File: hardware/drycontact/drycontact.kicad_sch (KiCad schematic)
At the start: 0 parts

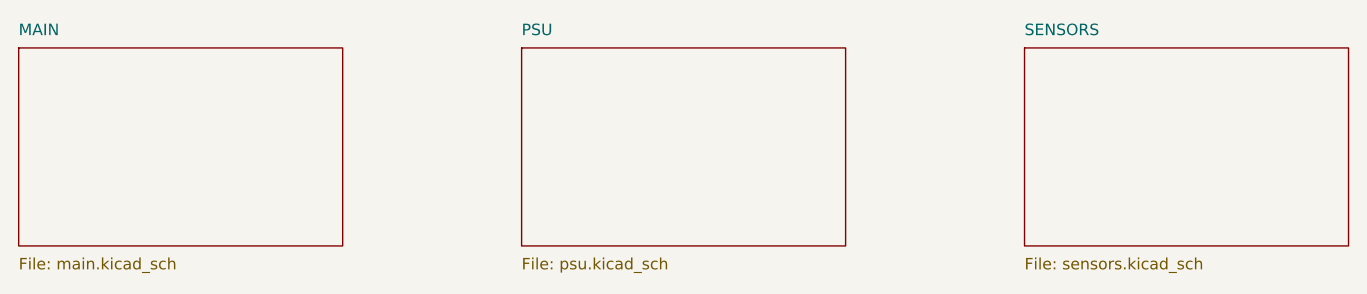
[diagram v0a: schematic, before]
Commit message: hardware: place parts for DryContact, PlugControl, SensorBuddy
Generate each board's schematic from a scripts/<board>.schgen.py manifest —
every part resolves to a real KiCad symbol + matching footprint + 3D model + LCSC.
Parts are PLACED, not wired (wire in eeschema; each sheet carries a pinout note).
make check-<board> = structure sound for all three:
- DryContact  (NEW): 49 components — STM32G0B1 + TCAN1044 + ULN2003 + 4x Omron
  G6K-2F-Y Form-C dry contacts; 29-bit CAN, UID auto-address. + BOM + handsolder.
- PlugControl (NEW KiCad project): 88 components — mcu/safety/actuation. A few
  generic stand-in symbols (TLV3202/74HC08/REF3330/TPS3823/SSR) pending swap;
  footprints/LCSC are correct.
- SensorBuddy (regenerated from placeholders): 81 components — ESP32-S3 + STM32G0B1
  + isolated ADM3260/ADS1115/OPA2376 probe front-end + NTC/1-Wire/floats.
Reuses the existing custom symbols in lib/symbols/sensorbuddy.kicad_sym.

Co-Authored-By: Claude Opus 4.8 (1M context) <noreply@anthropic.com>
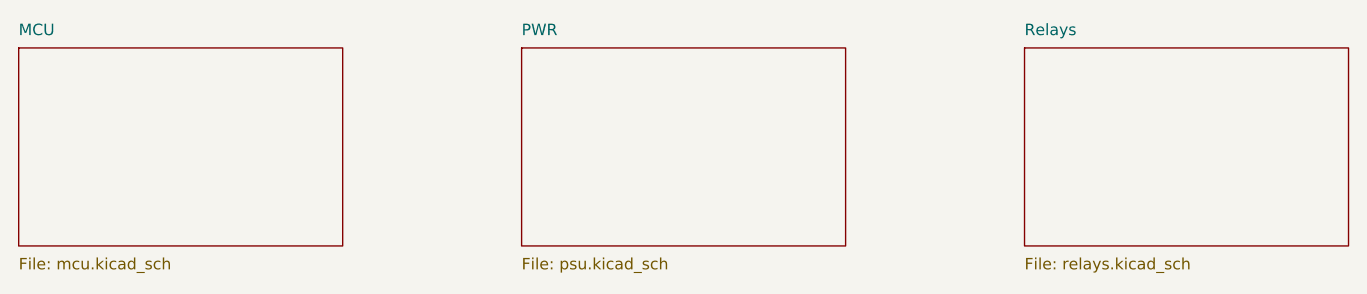
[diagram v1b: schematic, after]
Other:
- removed sheet MAIN
- removed sheet PSU
- removed sheet SENSORS
- added sheet MCU (mcu.kicad_sch)
- added sheet PWR (psu.kicad_sch)
- added sheet Relays (relays.kicad_sch)
- title: ReefVolt SensorBuddy — Main -> ReefVolt DryContact — 4ch Form-C carrier
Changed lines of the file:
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@@
 	(paper "A3")
 	(title_block
-		(title "ReefVolt SensorBuddy — Main")
+		(title "ReefVolt DryContact — 4ch Form-C carrier")
 		(date "2026-07-04")
 		(rev "0.1")
 		(company "blueAcro / ReefVolt")
-		(comment 1 "Aquarium sensor interface — CAN master of the SensorBuddy cluster")
-		(comment 2 "ESP32-S3 + STM32G0B1 + isolated pH/ORP + NTC + 1-Wire + floats")
+		(comment 1 "4-channel Form-C dry-contact output carrier for the SensorBuddy CAN cluster")
+		(comment 2 "STM32G0B1 + TCAN1044 + ULN2003 + 4x Omron G6K-2F-Y; 29-bit CAN, UID auto-address")
 	)
 	(sheet
@@
 		(stroke (width 0.1524) (type solid))
 		(fill (color 0 0 0 0.0000))
-		(property "Sheetname" "MAIN"
+		(property "Sheetname" "MCU"
 			(at 40.64 39.37 0)
 			(effects (font (size 1.27 1.27)) (justify left bottom))
 		)
-		(property "Sheetfile" "main.kicad_sch"
+		(property "Sheetfile" "mcu.kicad_sch"
 			(at 40.64 63.91 0)
 			(effects (font (size 1.27 1.27)) (justify left top))
@@
 		(stroke (width 0.1524) (type solid))
 		(fill (color 0 0 0 0.0000))
-		(property "Sheetname" "PSU"
+		(property "Sheetname" "PWR"
 			(at 96.52 39.37 0)
 			(effects (font (size 1.27 1.27)) (justify left bottom))
@@
 		(stroke (width 0.1524) (type solid))
 		(fill (color 0 0 0 0.0000))
-		(property "Sheetname" "SENSORS"
+		(property "Sheetname" "Relays"
 			(at 152.40 39.37 0)
 			(effects (font (size 1.27 1.27)) (justify left bottom))
 		)
-		(property "Sheetfile" "sensors.kicad_sch"
+		(property "Sheetfile" "relays.kicad_sch"
 			(at 152.40 63.91 0)
 			(effects (font (size 1.27 1.27)) (justify left top))
